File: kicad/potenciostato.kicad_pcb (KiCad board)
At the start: 2 copper layers, 150 x 100 mm, 45 parts, among them J1 Conn_01x03_Female, J3 Conn_01x03_Male, U1 OP77, U2 TL082, U3 OP77, U4 OP77, U5 4016, U6 4016, U7 LM324, U8 4016

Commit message: merge pcb 2/2/21 con ultima version
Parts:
- removed C1, C2: C, Capacitor_THT:C_Axial_L5.1mm_D3.1mm_P10.00mm_Horizontal
- added R24: R, Resistor_THT:R_Axial_DIN0207_L6.3mm_D2.5mm_P7.62mm_Horizontal, F.Cu at (767.6, 58.4)
- added R25: R, Resistor_THT:R_Axial_DIN0207_L6.3mm_D2.5mm_P7.62mm_Horizontal, F.Cu at (767.6, 61.5)
- added R26: R, Resistor_THT:R_Axial_DIN0207_L6.3mm_D2.5mm_P7.62mm_Horizontal, F.Cu at (702.3, 33.8)
- added R27: R, Resistor_THT:R_Axial_DIN0207_L6.3mm_D2.5mm_P7.62mm_Horizontal, F.Cu at (702.3, 54.9)
- added RV11: R_POT, Potentiometer_THT:Potentiometer_Bourns_3266Y_Vertical, F.Cu at (782.5, 62.4)
- added RV12: R_POT, Potentiometer_THT:Potentiometer_Bourns_3266Y_Vertical, F.Cu at (702.3, 38.1)
- U7: value LM324 -> TL064
- moved J1 22.4 mm to (656.6, 33.8), turned to 270 degrees
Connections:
- R7 pad 2: (no net) -> Net-(R7-Pad2)
- U5 pad 12: (no net) -> /salida_dac/OFF_I_2
- U5 pad 6: (no net) -> /salida_dac/OFF_I_1
- U6 pad 10: Net-(C1-Pad2) -> Net-(R7-Pad2)
- U6 pad 11: Net-(R6-Pad1) -> Net-(RV11-Pad2)
- U6 pad 12: (no net) -> /salida_dac/OFF_I_2
- U6 pad 6: (no net) -> /salida_dac/OFF_I_1
- U6 pad 8: Net-(R6-Pad1) -> Net-(RV12-Pad2)
- U6 pad 9: Net-(C2-Pad2) -> Net-(R7-Pad2)
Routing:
- net -5V: track 78.2 -> 224.3 mm, vias 0 -> 2
- net +5V: track 251.5 -> 269.1 mm
- net Net-(C1-Pad2): track 6.13 -> 0.00 mm
- net Net-(C2-Pad2): track 5.24 -> 0.00 mm
- net Net-(R26-Pad1): track 0.00 -> 4.32 mm
- net Net-(R27-Pad2): track 0.00 -> 4.06 mm
- added copper zone on B.Cu, net GND

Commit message: continuacion ruteo pcb
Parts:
- moved R14 86.3 mm to (732.0, 77.0), turned to 270 degrees
- moved RV2 74.4 mm to (727.2, 71.9), turned to 90 degrees
- moved R9 69.9 mm to (727.2, 68.8), turned to 180 degrees
- moved R25 30.9 mm to (742.2, 43.9)
- moved RV11 30.5 mm to (755.1, 49.0), turned to 270 degrees
- moved R24 19.9 mm to (750.1, 49.0), turned to 180 degrees
- moved R26 9.16 mm to (707.4, 41.4)
- moved R12 4.83 mm to (674.4, 34.5)
- moved R13 4.83 mm to (674.4, 29.5)
- moved R27 4.83 mm to (702.3, 50.0)
- moved RV12 4.83 mm to (702.3, 33.3)
- moved RV4 4.83 mm to (674.4, 39.6)
- moved RV5 4.83 mm to (674.4, 24.4)
- moved U6 4.83 mm to (685.8, 26.9)
- moved R6 3.42 mm to (672.8, 55.9), turned to 90 degrees
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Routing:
- net Net-(RV11-Pad2): track 0.00 -> 90.8 mm
- net /salida_dac/OFF_I_1: track 0.00 -> 46.0 mm
- net /salida_dac/OFF_I_2: track 0.00 -> 43.9 mm
- net Net-(R7-Pad2): track 0.00 -> 38.0 mm, vias 0 -> 2
- net Net-(R9-Pad2): track 0.00 -> 25.0 mm
- net Net-(U5-Pad10): track 37.0 -> 14.2 mm
- net /salida_dac/V_IN: track 85.0 -> 99.0 mm
- net Net-(RV12-Pad2): track 0.00 -> 10.5 mm
- net Net-(R3-Pad2): track 5.64 -> 15.4 mm
- net Net-(R6-Pad1): track 40.0 -> 48.1 mm
- net -5V: track 224.3 -> 232.0 mm
- net Net-(R14-Pad1): track 15.5 -> 22.9 mm
- net /salida_dac/VIN: track 76.8 -> 69.5 mm
- net Net-(R26-Pad1): track 4.32 -> 10.8 mm
- net +5V: track 269.1 -> 263.8 mm
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
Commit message: Add files via upload
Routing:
- net +5V: track 263.8 -> 378.8 mm, vias 0 -> 1
- net Net-(J3-Pad3): track 0.00 -> 95.9 mm
- net GND: track 79.7 -> 133.6 mm
- net Net-(R2-Pad1): track 26.9 -> 77.6 mm
- net Net-(R1-Pad1): track 0.00 -> 50.0 mm
- net Net-(U5-Pad10): track 14.2 -> 58.8 mm
- net Net-(R4-Pad1): track 12.6 -> 43.4 mm
- net -5V: track 232.0 -> 252.5 mm
- net /salida_dac/I_IN: track 0.00 -> 15.4 mm
- net Net-(R12-Pad2): track 0.00 -> 3.81 mm
- net /salida_dac/V_IN: track 99.0 -> 101.6 mm
- net Net-(R3-Pad2): track 15.4 -> 17.9 mm
- net Net-(U7-Pad5): track 49.1 -> 49.8 mm

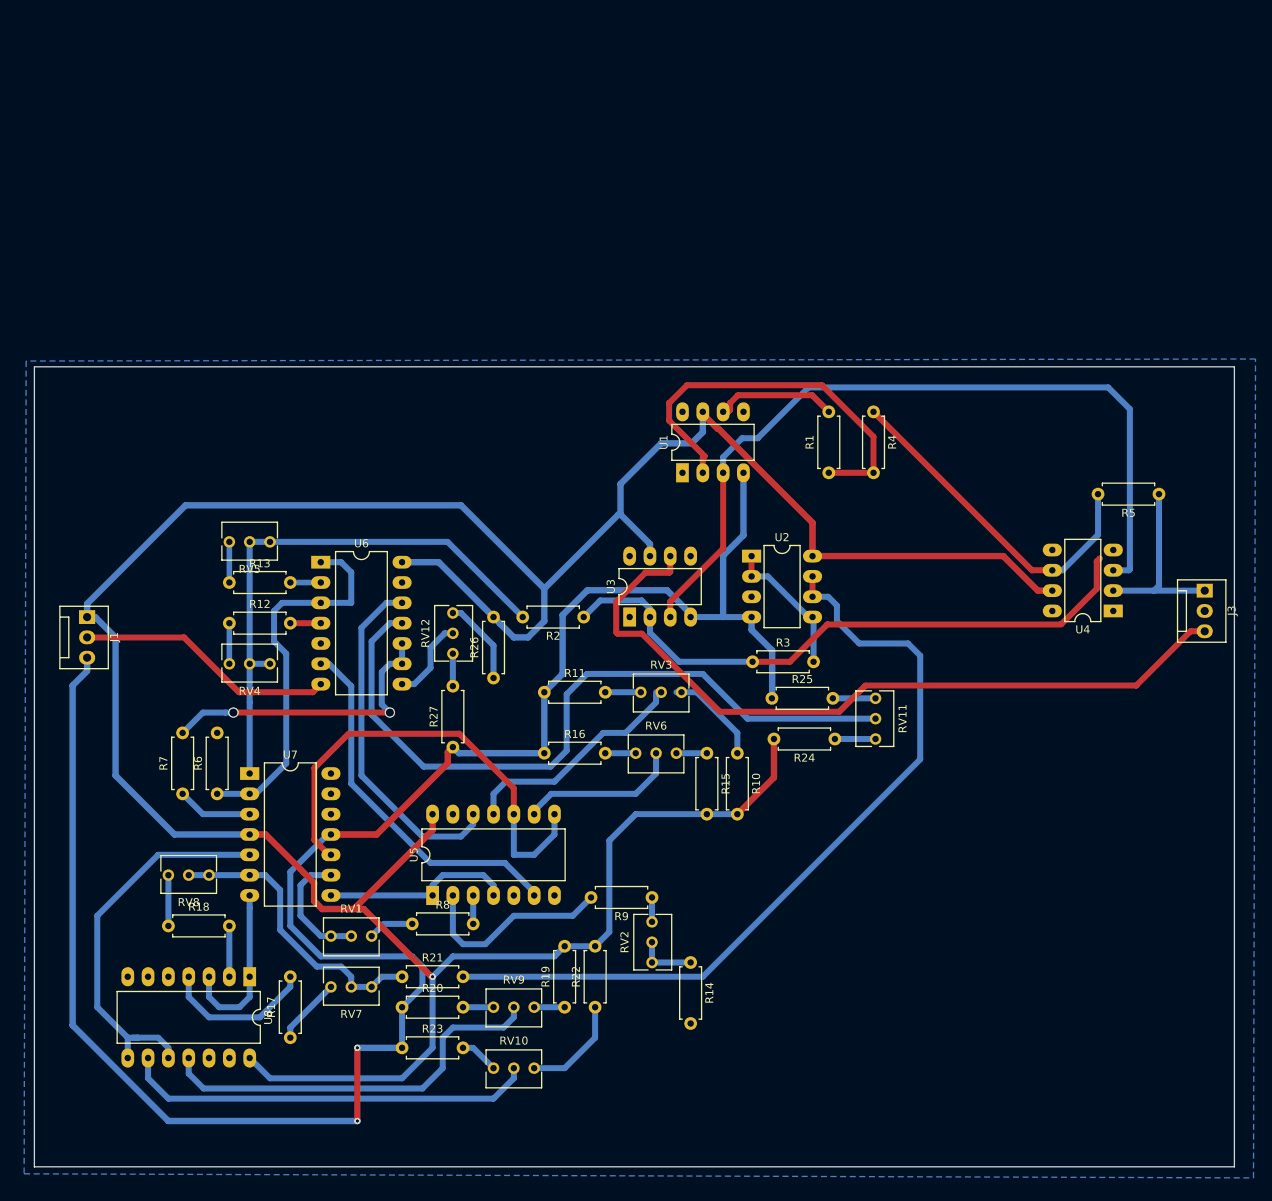
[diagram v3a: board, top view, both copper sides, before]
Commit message: agregada huella del lpc al pcb
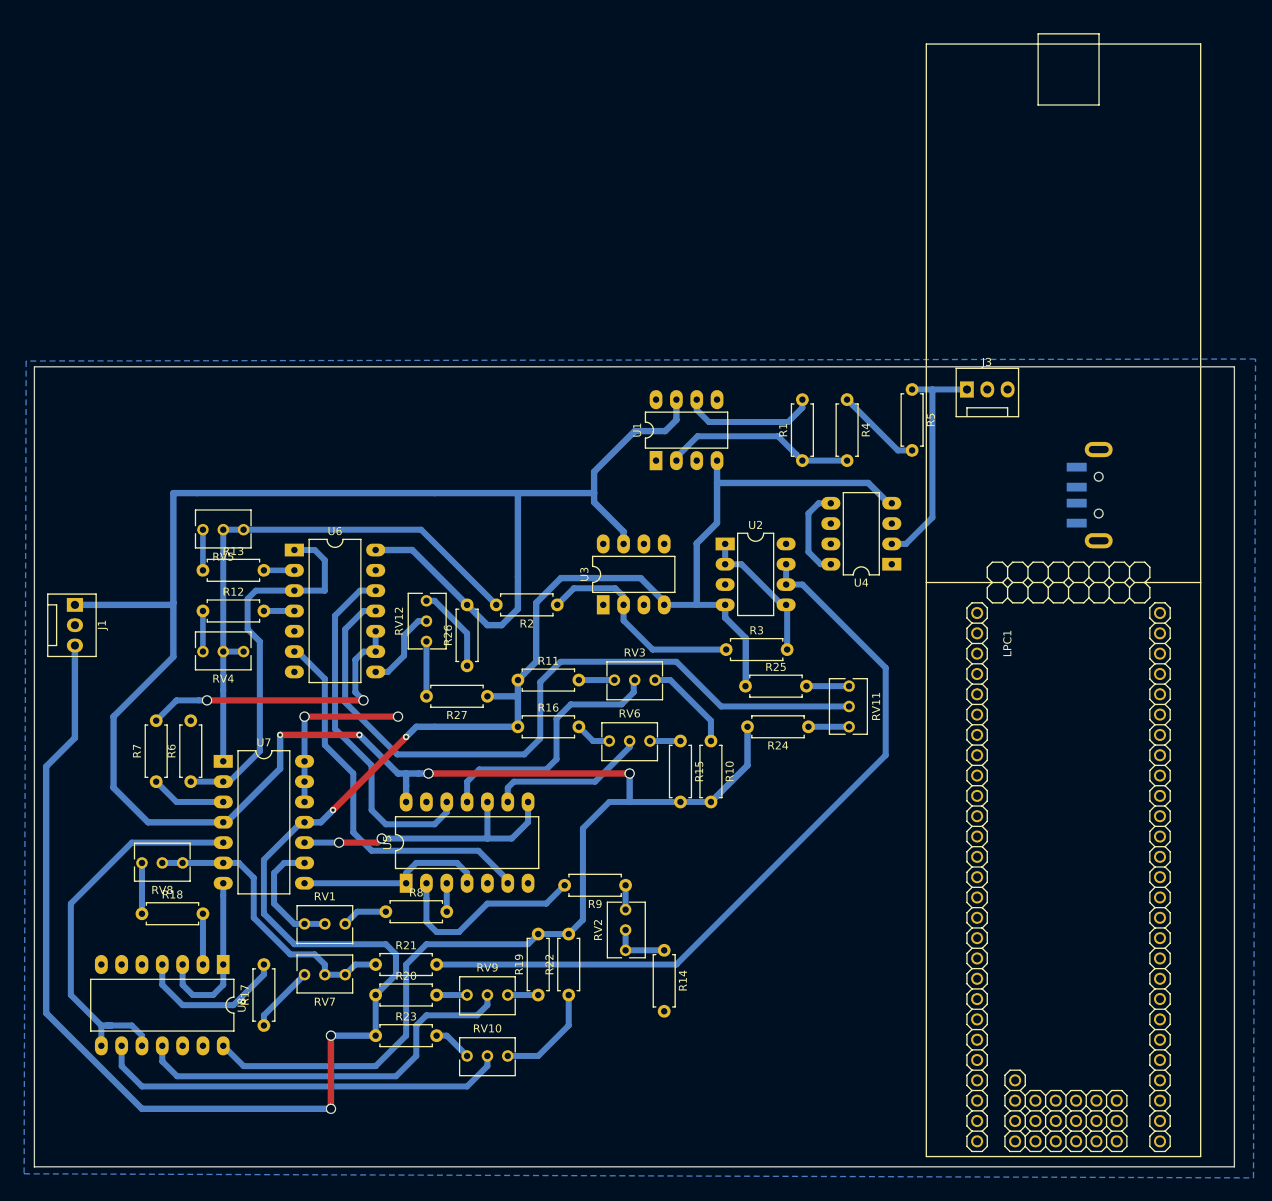
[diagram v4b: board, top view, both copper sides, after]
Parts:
- added J2: USB_B_Micro, Connector_USB:USB_A_CNCTech_1001-011-01101_Horizontal, B.Cu at (789.9, 18.5)
- added LPC1: LPCXPRESSO_LPC1769, LPC:LPCXPRESSO_LPC1769, F.Cu at (773.6, -0.38)
- moved J3 38.9 mm to (766.6, 5.33), turned to 0 degrees
- moved R5 33.5 mm to (759.7, 5.33), turned to 270 degrees
- moved U4 28.3 mm to (757.2, 27.2)
- moved R27 7.68 mm to (706.6, 43.7), turned to 180 degrees
- moved R16 4.67 mm to (710.4, 47.5)
- moved R11 3.64 mm to (710.4, 41.7)
- moved R14 3.64 mm to (728.7, 75.4)
- moved R17 3.64 mm to (678.7, 84.8)
- moved R18 3.64 mm to (663.4, 70.9)
- moved R19 3.64 mm to (713.0, 81.0)
- moved R20 3.64 mm to (692.7, 81.0)
- moved R21 3.64 mm to (692.7, 77.2)
- moved R22 3.64 mm to (716.8, 81.0)
- moved R23 3.64 mm to (692.7, 86.1)
- moved R24 3.64 mm to (746.8, 47.5)
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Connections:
- net /salida_dac/I_ADC renamed /LPC/ADC0
- net /salida_dac/V_ADC renamed /LPC/ADC1
- R6 pad 2: (no net) -> /LPC/DAC
- U5 pad 13: (no net) -> /LPC/P0.3
- U5 pad 5: (no net) -> /LPC/P0.2
- U6 pad 13: (no net) -> /LPC/P2.2
- U6 pad 5: (no net) -> /LPC/P2.1
- U8 pad 12: (no net) -> /salida_dac/OFF_V_2
- U8 pad 13: (no net) -> /LPC/P2.6
- U8 pad 5: (no net) -> /LPC/P2.5
- U8 pad 6: (no net) -> /salida_dac/OFF_V_1
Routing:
- net GND: track 133.6 -> 23.0 mm, vias 0 -> 2
- net Net-(J3-Pad3): track 95.9 -> 0.00 mm
- net Net-(R2-Pad1): track 77.6 -> 26.9 mm
- net Net-(R4-Pad1): track 43.4 -> 10.9 mm
- net +5V: track 378.8 -> 349.8 mm, vias 1 -> 4
- net Net-(R1-Pad1): track 50.0 -> 24.1 mm
- net -5V: track 252.5 -> 278.1 mm, vias 2 -> 4
- net Net-(U5-Pad10): track 58.8 -> 36.5 mm, vias 0 -> 2
- net (no net): track 0.00 -> 11.6 mm
- net Net-(J3-Pad1): track 23.1 -> 29.3 mm
- net /salida_dac/V_IN: track 101.6 -> 97.2 mm
- net Net-(RV3-Pad2): track 28.9 -> 32.5 mm
- net Net-(R27-Pad2): track 4.06 -> 6.86 mm
- net /salida_dac/OFF_I_1: track 46.0 -> 48.1 mm
- net /salida_dac/I_IN: track 15.4 -> 16.9 mm
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
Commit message: Prueba Gus
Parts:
- moved LPC1 6.23 mm to (779.8, -0.64)

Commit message: kicad
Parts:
- J2: moved to F.Cu
- moved J2 37.5 mm to (803.9, 53.3)
- moved R5 17.5 mm to (742.3, 6.99)
- moved J3 15.6 mm to (751.2, 8.26), turned to 270 degrees
- moved R1 13.4 mm to (732.7, 14.9)
- moved R4 13.4 mm to (738.3, 7.24)
- moved LPC1 11.0 mm to (769.0, -2.54)
- moved U1 10.9 mm to (716.9, 15.9)
- moved R2 8.86 mm to (711.8, 24.1)
- moved U2 4.45 mm to (731.9, 24.6)
- moved U3 4.45 mm to (716.7, 32.3)
- moved U4 4.44 mm to (752.7, 27.2)
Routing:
- net Net-(J3-Pad1): track 29.3 -> 0.18 mm
- net +5V: track 349.8 -> 321.0 mm
- net Net-(R2-Pad1): track 26.9 -> 0.00 mm
- net GND: track 23.0 -> 42.9 mm
- net Net-(R1-Pad1): track 24.1 -> 6.72 mm
- net /salida_dac/I_IN: track 16.9 -> 1.02 mm
- net -5V: track 278.1 -> 266.4 mm
- net Net-(R4-Pad1): track 10.9 -> 0.00 mm
- net /salida_dac/VIN: track 69.5 -> 62.0 mm
- net Net-(R3-Pad2): track 17.9 -> 12.4 mm
- net /salida_dac/V_IN: track 97.2 -> 101.6 mm
- net (no net): track 11.6 -> 13.9 mm

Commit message: kicad
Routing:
- net +5V: track 321.0 -> 347.7 mm
- net /salida_dac/I_IN: track 1.02 -> 14.2 mm
- net Net-(J3-Pad1): track 0.18 -> 9.60 mm
- net Net-(R4-Pad1): track 0.00 -> 9.05 mm
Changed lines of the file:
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@@
     (thickness 1.6)
     (drawings 4)
-    (tracks 333)
+    (tracks 348)
     (zones 0)
     (modules 51)
@@
   (segment (start 667.371 18.288) (end 667.371 32.004) (width 0.8) (layer B.Cu) (net 1))
   (segment (start 667.371 32.004) (end 667.371 38.749) (width 0.8) (layer B.Cu) (net 1))
-  (segment (start 710.438 18.288) (end 718.058 18.288) (width 0.8) (layer B.Cu) (net 1))
   (segment (start 723.646 23.876) (end 723.646 24.638) (width 0.8) (layer B.Cu) (net 0))
   (segment (start 708.533 34.798) (end 708.787 34.544) (width 0.8) (layer B.Cu) (net 1))
   (segment (start 706.628 34.798) (end 708.533 34.798) (width 0.8) (layer B.Cu) (net 1))
   (segment (start 704.088 32.258) (end 706.628 34.798) (width 0.8) (layer B.Cu) (net 1))
-  (segment (start 708.787 18.288) (end 710.438 18.288) (width 0.8) (layer B.Cu) (net 1))
   (segment (start 708.787 34.544) (end 708.787 18.288) (width 0.8) (layer B.Cu) (net 1))
   (segment (start 700.024 18.288) (end 708.787 18.288) (width 0.8) (layer B.Cu) (net 1))
+  (segment (start 719.455 24.384) (end 719.201 24.638) (width 0.8) (layer B.Cu) (net 1))
+  (segment (start 719.455 19.685) (end 719.455 24.384) (width 0.8) (layer B.Cu) (net 1))
+  (segment (start 718.058 18.288) (end 719.455 19.685) (width 0.8) (layer B.Cu) (net 1))
+  (segment (start 708.787 18.288) (end 718.058 18.288) (width 0.8) (layer B.Cu) (net 1))
+  (segment (start 708.787 18.288) (end 708.787 11.938) (width 0.8) (layer B.Cu) (net 1))
+  (segment (start 708.787 11.938) (end 709.295 11.43) (width 0.8) (layer B.Cu) (net 1))
+  (segment (start 719.455 10.255) (end 719.455 8.255) (width 0.8) (layer B.Cu) (net 1))
+  (segment (start 718.28 11.43) (end 719.455 10.255) (width 0.8) (layer B.Cu) (net 1))
+  (segment (start 709.295 11.43) (end 718.28 11.43) (width 0.8) (layer B.Cu) (net 1))
   (segment (start 678.688 64.116) (end 683.368 59.436) (width 0.75) (layer B.Cu) (net 2))
   (segment (start 683.368 59.436) (end 683.768 59.436) (width 0.75) (layer B.Cu) (net 2))
@@
   (segment (start 731.901 24.638) (end 731.901 27.178) (width 0.75) (layer B.Cu) (net 8))
   (segment (start 742.696 7.239) (end 742.823 7.366) (width 0.75) (layer F.Cu) (net 5))
+  (segment (start 749.935 6.985) (end 751.205 8.255) (width 0.75) (layer B.Cu) (net 5))
+  (segment (start 742.315 6.985) (end 749.935 6.985) (width 0.75) (layer B.Cu) (net 5))
+  (segment (start 742.315 11.303) (end 738.251 7.239) (width 0.75) (layer B.Cu) (net 9))
+  (segment (start 742.315 14.605) (end 742.315 11.303) (width 0.75) (layer B.Cu) (net 9))
   (segment (start 682.498 25.4) (end 685.038 25.4) (width 0.75) (layer B.Cu) (net 10))
   (segment (start 685.038 25.4) (end 686.308 26.67) (width 0.75) (layer B.Cu) (net 10))
@@
   (segment (start 698.34 22.86) (end 702.31 22.86) (width 0.75) (layer B.Cu) (net 38))
   (segment (start 702.31 22.86) (end 703.58 24.13) (width 0.75) (layer B.Cu) (net 38))
-  (segment (start 737.108 8.255) (end 737.108 7.239) (width 0.75) (layer B.Cu) (net 39))
+  (segment (start 730.885 5.08) (end 732.663 6.858) (width 0.75) (layer B.Cu) (net 39))
+  (segment (start 723.22 5.08) (end 730.885 5.08) (width 0.75) (layer B.Cu) (net 39))
+  (segment (start 732.663 6.858) (end 732.663 7.239) (width 0.75) (layer B.Cu) (net 39))
+  (segment (start 721.995 6.305) (end 723.22 5.08) (width 0.75) (layer B.Cu) (net 39))
+  (segment (start 721.995 8.255) (end 721.995 6.305) (width 0.75) (layer B.Cu) (net 39))
   (segment (start 739.521 27.178) (end 739.521 29.718) (width 0.75) (layer B.Cu) (net 40))
   (segment (start 756.412 51.054) (end 730.25 77.216) (width 0.75) (layer B.Cu) (net 40))

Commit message: kicad
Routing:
- net Net-(R2-Pad1): track 0.00 -> 40.2 mm, vias 0 -> 2
- net GND: track 42.9 -> 5.71 mm, vias 2 -> 0
- net Net-(J3-Pad1): track 9.60 -> 31.2 mm
- net Net-(R1-Pad1): track 6.72 -> 22.6 mm
- net Net-(R4-Pad1): track 9.05 -> 24.8 mm, vias 0 -> 3
- net -5V: track 266.4 -> 281.9 mm
- net (no net): track 13.9 -> 0.00 mm
- net Net-(R3-Pad2): track 12.4 -> 19.9 mm
